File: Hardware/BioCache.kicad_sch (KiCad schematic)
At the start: 0 parts

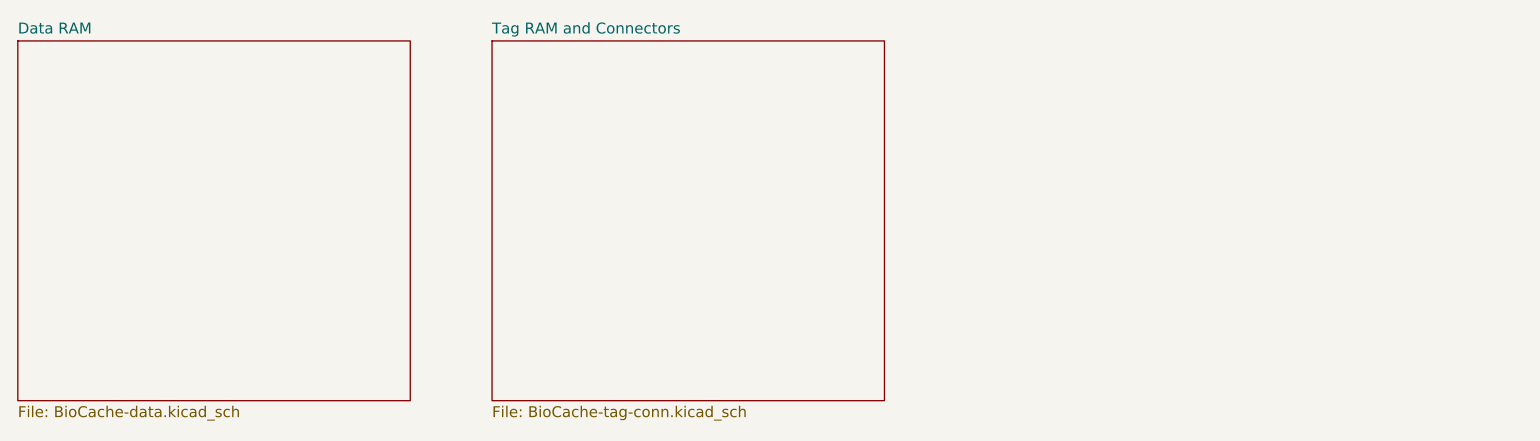
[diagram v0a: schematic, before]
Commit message: Upgrade to KiCad 9, clean-up schematics, set up KiBot
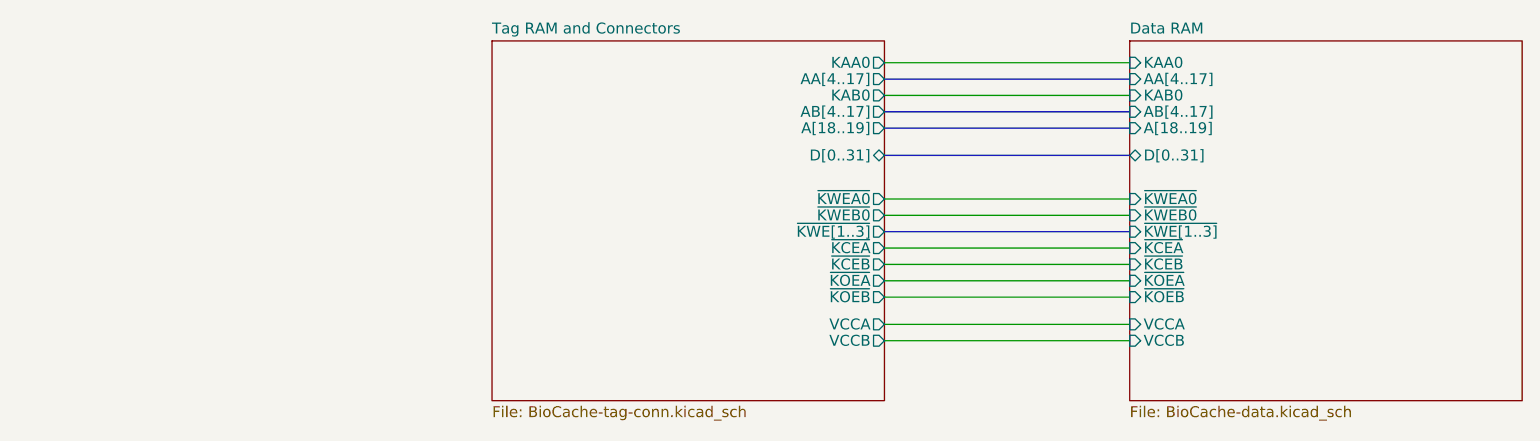
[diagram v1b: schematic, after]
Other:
- sheet Data RAM ports: added AA[4..17], AB[4..17], A[18..19], D[0..31], KAA0, KAB0, VCCA, VCCB, ~{KCEA}, ~{KCEB}, ~{KOEA}, ~{KOEB}, ~{KWEA0}, ~{KWEB0}, ~{KWE[1..3]}; removed none
- sheet Tag RAM and Connectors ports: added AA[4..17], AB[4..17], A[18..19], D[0..31], KAA0, KAB0, VCCA, VCCB, ~{KCEA}, ~{KCEB}, ~{KOEA}, ~{KOEB}, ~{KWEA0}, ~{KWEB0}, ~{KWE[1..3]}; removed none
- title: (none) -> Biostar MB-84xx-UUD 1MB cache module
